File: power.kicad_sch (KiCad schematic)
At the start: 23 parts, among them IC5 BQ24074RGTR, IC6 LP2985-30DBVR, IC7 NCP718ASN300T1G, J4 217175-0001

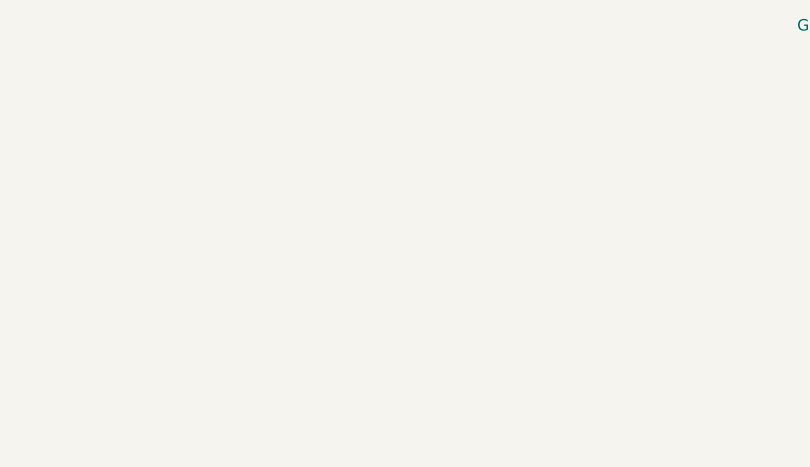
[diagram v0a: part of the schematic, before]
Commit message: Added FPGA power component
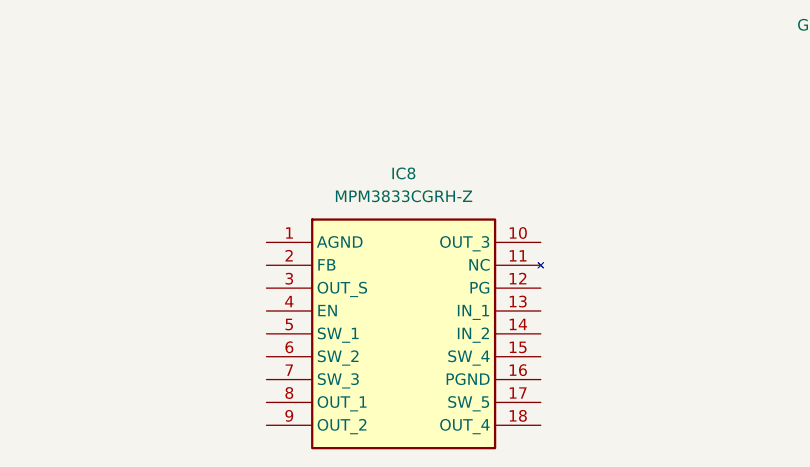
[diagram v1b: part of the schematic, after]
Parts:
- added IC8: MPM3833CGRH-Z, MPM3833CGRHP, symbol SamacSys_Parts:MPM3833CGRH-Z
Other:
- title: (none) -> Power
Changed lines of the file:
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@@
 (kicad_sch (version 20230121) (generator eeschema)
   (paper "A4")
+  (title_block
+    (title "Power")
+  )
   (junction (at 111.76 132.08) (diameter 0) (color 0 0 0 0)
   )
@@
         )
       )
+    )
+  )
+  (symbol (lib_id "SamacSys_Parts:MPM3833CGRH-Z") (at 50.8 163.83 0) (unit 1)
+    (in_bom yes) (on_board yes) (dnp no) (fields_autoplaced)
+    (property "Reference" "IC8" (at 66.04 156.21 0)
+      (effects (font (size 1.27 1.27)))
+    )
+    (property "Value" "MPM3833CGRH-Z" (at 66.04 158.75 0)
+      (effects (font (size 1.27 1.27)))
+    )
+    (property "Footprint" "MPM3833CGRHP" (at 77.47 258.75 0)
+      (effects (font (size 1.27 1.27)) (justify left top) hide)
+    )
+    (property "Datasheet" "https://www.monolithicpower.com/en/mpm3833c.html" (at 77.47 358.75 0)
+      (effects (font (size 1.27 1.27)) (justify left top) hide)
+    )
+    (property "Height" "1.65" (at 77.47 558.75 0)
+      (effects (font (size 1.27 1.27)) (justify left top) hide)
+    )
+    (property "Mouser Part Number" "946-MPM3833CGRH-Z" (at 77.47 658.75 0)
+      (effects (font (size 1.27 1.27)) (justify left top) hide)
+    )
+    (property "Mouser Price/Stock" "https://www.mouser.co.uk/ProductDetail/Monolithic-Power-Systems-MPS/MPM3833CGRH-Z?qs=l7cgNqFNU1hClq0DBZDZVg%3D%3D" (at 77.47 758.75 0)
+      (effects (font (size 1.27 1.27)) (justify left top) hide)
+    )
+    (property "Manufacturer_Name" "Monolithic Power Systems (MPS)" (at 77.47 858.75 0)
+      (effects (font (size 1.27 1.27)) (justify left top) hide)
+    )
+    (property "Manufacturer_Part_Number" "MPM3833CGRH-Z" (at 77.47 958.75 0)
+      (effects (font (size 1.27 1.27)) (justify left top) hide)
+    )
+    (pin "12")
+    (pin "7")
+    (pin "16")
+    (pin "2")
+    (pin "1")
+    (pin "18")
+    (pin "17")
+    (pin "6")
+    (pin "13")
+    (pin "8")
+    (pin "9")
+    (pin "14")
+    (pin "3")
+    (pin "4")
+    (pin "11")
+    (pin "5")
+    (pin "15")
+    (pin "10")
+    (instances
+      (project "drone"
+        (path "/d34d8324-c983-4098-8d7e-5c2fbd34794d/f990703e-099d-439c-9e1d-875871db40e1"
+          (reference "IC8") (unit 1)
+        )
+      )

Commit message: Prepare for power curcuit changes
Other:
- moved on the sheet: IC8, J4, J?, R15, R16

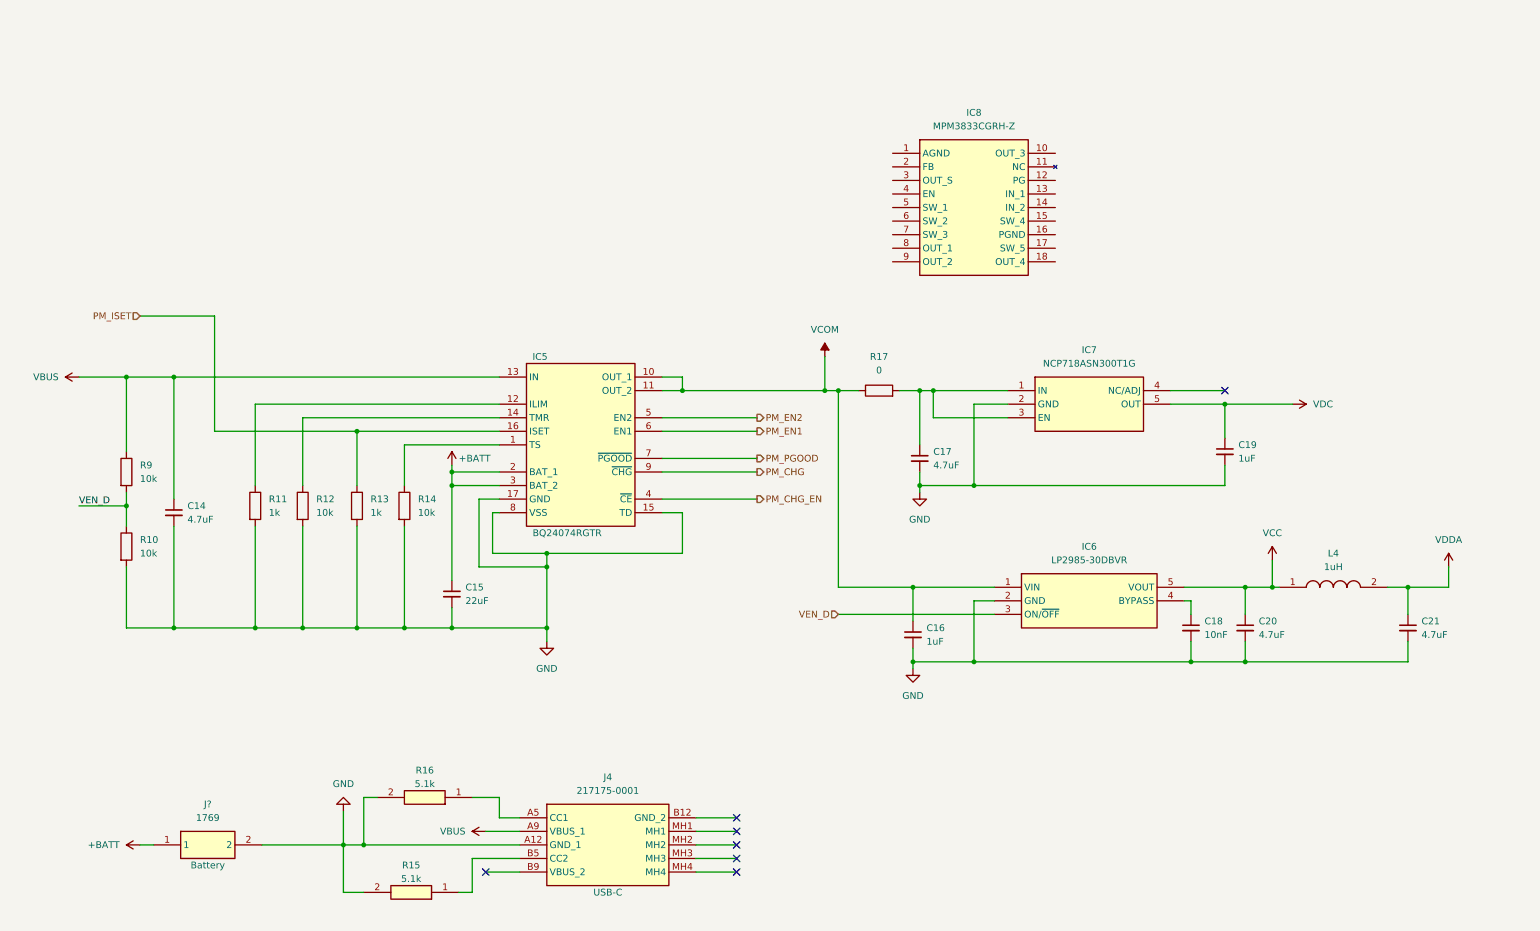
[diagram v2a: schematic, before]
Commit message: Integrated MPM3833C
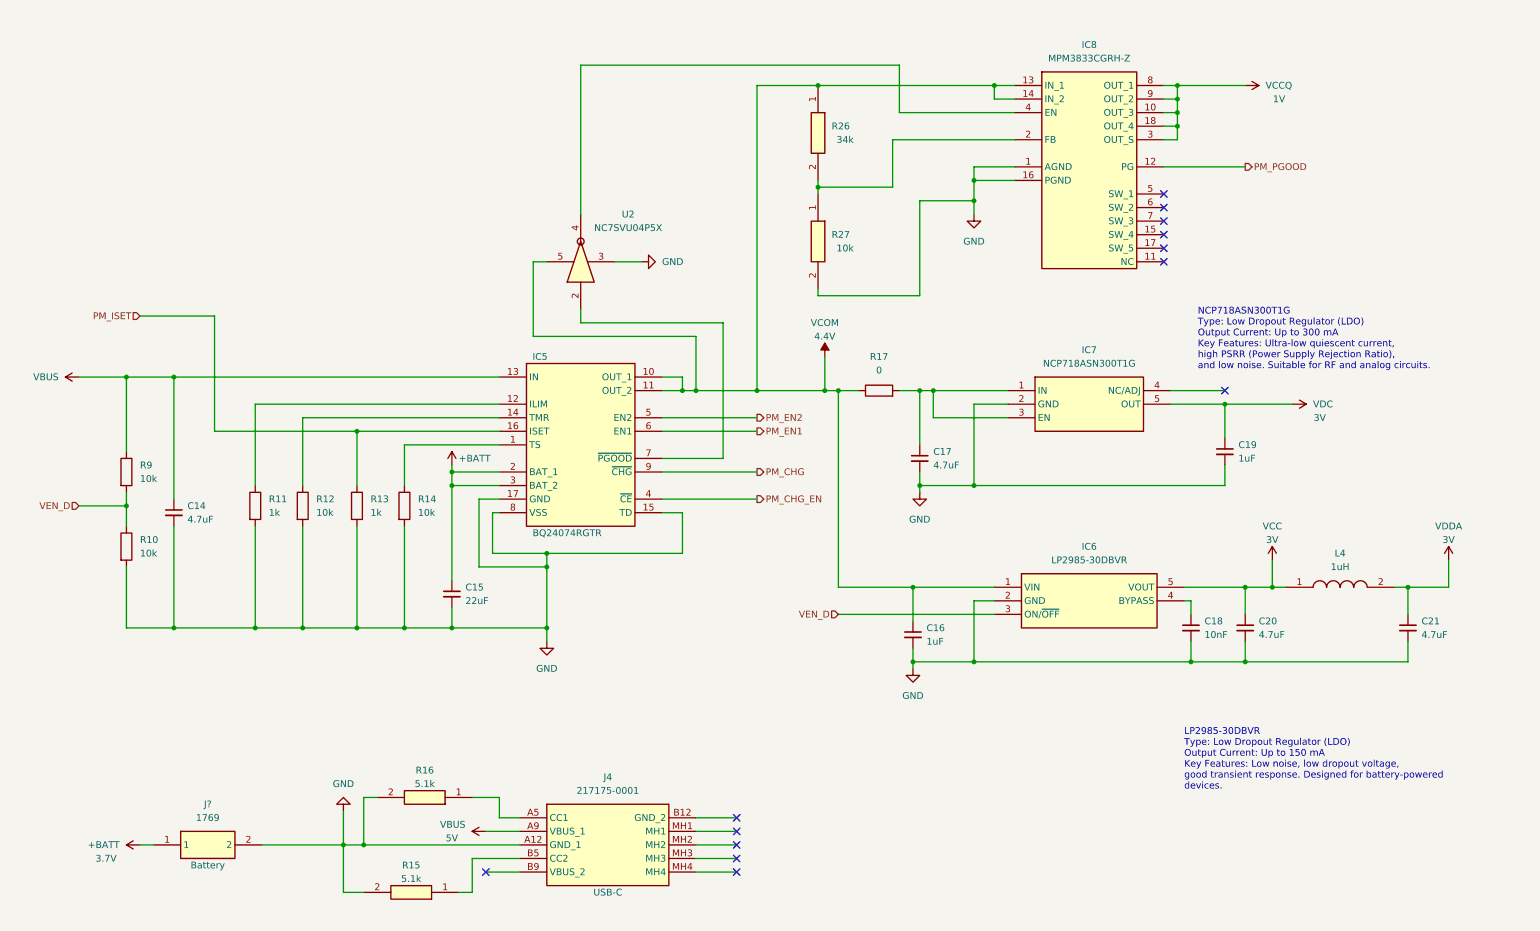
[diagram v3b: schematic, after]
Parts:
- added R26: ERA-2ARB3402X, ERA2AED122X, symbol SamacSys_Parts:ERA-2ARB3402X
- added R27: ERA-8VRB1002V, ERA8KEB1004V, symbol SamacSys_Parts:ERA-8VRB1002V
- added U2: NC7SVU04P5X, Package_TO_SOT_SMD:SOT-353_SC-70-5, symbol 74xGxx:NC7SVU04P5X
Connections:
- net GND: now also IC8.1 (AGND), IC8.16 (PGND), R27.2, U2.3
- net PM_PGOOD: now also IC8.12 (PG); no longer IC5.7 (~{PGOOD})
- net VCOM: now also IC8.13 (IN_1), IC8.14 (IN_2), R26.1, U2.5
- net VCCQ: now reaches IC8.10 (OUT_3)
- net VCCQ: now also IC8.18 (OUT_4), IC8.3 (OUT_S), IC8.8 (OUT_1), IC8.9 (OUT_2)
- net at IC8.2 (FB): now also R26.2, R27.1
- net at IC8.4 (EN): now also U2.4
- new net: IC5.7 (~{PGOOD}), U2.2
- no-connect marks 7 -> 13
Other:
- note added: "LP2985-30DBVR Type: Low Dropout Regulator (LDO) Output Current: Up to 150 mA Key Features: Low noise, low dropout voltage, good transient response. Designed for battery-powered devices."
- note added: "NCP718ASN300T1G Type: Low Dropout Regulator (LDO) Output Current: Up to 300 mA Key Features: Ultra-low quiescent current, high PSRR (Power Supply Rejection Ratio), and low noise. Suitable for RF and analog circuits."
- title: Power -> Power Management
- moved on the sheet: L4
